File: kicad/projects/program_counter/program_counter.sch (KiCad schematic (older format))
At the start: 47 parts, among them J1 Conn_01x16_Female, J2 Control_signal_backplane, J3 Bus_connection, J4 Aux_connection, J5 LED_CONTROL, J6 TOP_POWER, U1 74HC04, U2 74HC245, U3 74HC161, U4 74HC245, U5 74HC161, U6 74HC245, U7 74HC161, U8 74HC245, U9 74HC161

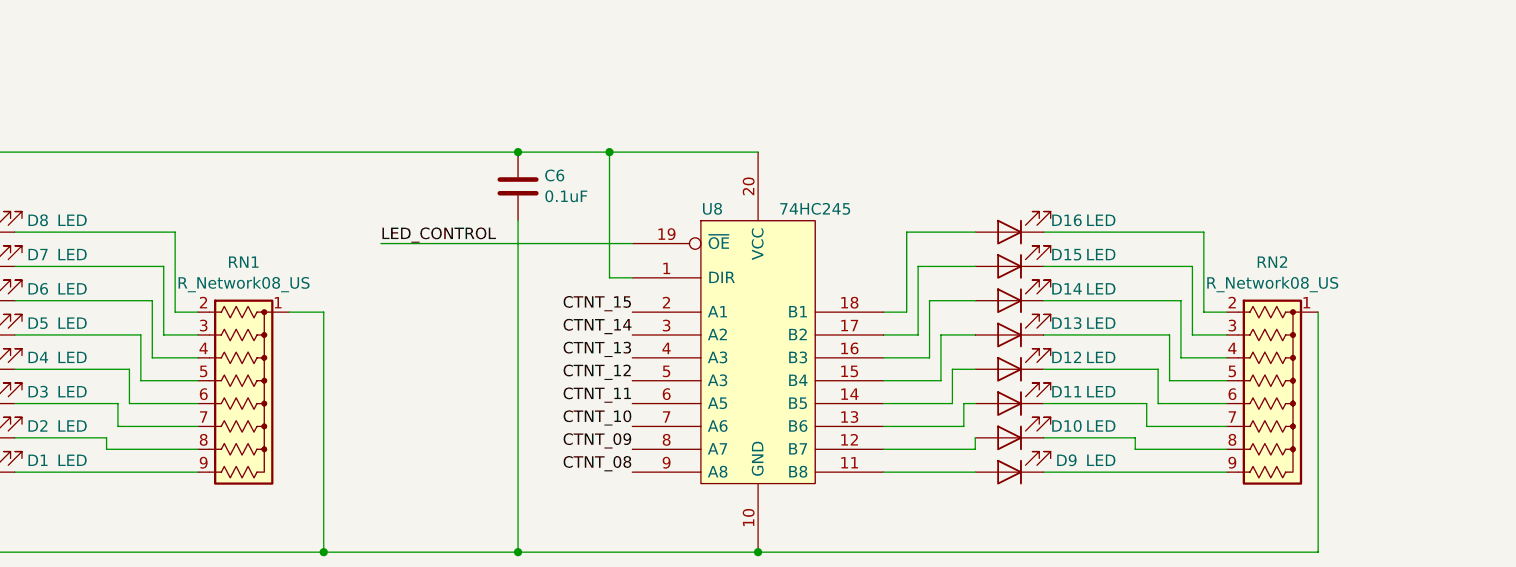
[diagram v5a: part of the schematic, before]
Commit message: Tech checks complete on program counter.
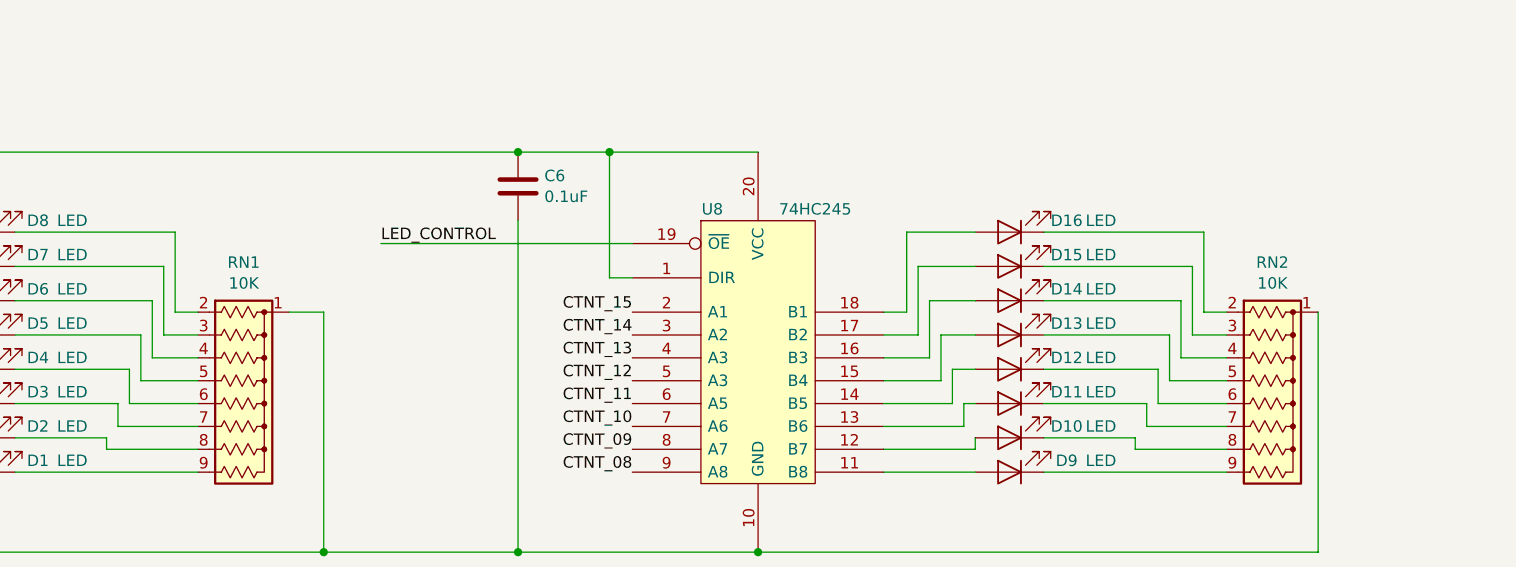
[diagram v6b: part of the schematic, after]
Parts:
- RN1, RN2: value R_Network08_US -> 10K
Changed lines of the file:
@@
 P 9200 9400
 F 0 "RN2" V 8583 9400 50  0000 C CNN
-F 1 "R_Network08_US" V 8674 9400 50  0000 C CNN
+F 1 "10K" V 8674 9400 50  0000 C CNN
 F 2 "Resistor_THT:R_Array_SIP9" V 9675 9400 50  0001 C CNN
 F 3 "http://www.vishay.com/docs/31509/csc.pdf" H 9200 9400 50  0001 C CNN
@@
 P 4700 9400
 F 0 "RN1" V 4083 9400 50  0000 C CNN
-F 1 "R_Network08_US" V 4174 9400 50  0000 C CNN
+F 1 "10K" V 4174 9400 50  0000 C CNN
 F 2 "Resistor_THT:R_Array_SIP9" V 5175 9400 50  0001 C CNN
 F 3 "http://www.vishay.com/docs/31509/csc.pdf" H 4700 9400 50  0001 C CNN

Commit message: Gerbers generated and zipped. Changed ICs to sockets.
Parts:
- U1: footprint Package_DIP:DIP-14_W7.62mm -> Package_DIP:DIP-14_W7.62mm_Socket
- U2, U4, U6, U8: footprint Package_DIP:DIP-20_W7.62mm -> Package_DIP:DIP-20_W7.62mm_Socket
- U3, U5, U7, U9: footprint Package_DIP:DIP-16_W7.62mm -> Package_DIP:DIP-16_W7.62mm_Socket
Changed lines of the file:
@@
 F 0 "U6" H 6450 6700 50  0000 C CNN
 F 1 "74HC245" H 6950 6700 50  0000 C CNN
-F 2 "Package_DIP:DIP-20_W7.62mm" H 6350 6000 50  0001 C CNN
+F 2 "Package_DIP:DIP-20_W7.62mm_Socket" H 6350 6000 50  0001 C CNN
 F 3 "" H 6350 6000 50  0001 C CNN
 	1    6700 6000
@@
 F 0 "U4" H 4400 6700 50  0000 C CNN
 F 1 "74HC245" H 4850 6700 50  0000 C CNN
-F 2 "Package_DIP:DIP-20_W7.62mm" H 4250 6000 50  0001 C CNN
+F 2 "Package_DIP:DIP-20_W7.62mm_Socket" H 4250 6000 50  0001 C CNN
 F 3 "" H 4250 6000 50  0001 C CNN
 	1    4600 6000
@@
 F 0 "U1" H 1400 3417 50  0000 C CNN
 F 1 "74HC04" H 1400 3326 50  0000 C CNN
-F 2 "Package_DIP:DIP-14_W7.62mm" H 1400 3100 50  0001 C CNN
+F 2 "Package_DIP:DIP-14_W7.62mm_Socket" H 1400 3100 50  0001 C CNN
 F 3 "https://assets.nexperia.com/documents/data-sheet/74HC_HCT04.pdf" H 1400 3100 50  0001 C CNN
 	1    1400 3100
@@
 F 0 "U1" H 1400 3967 50  0000 C CNN
 F 1 "74HC04" H 1400 3876 50  0000 C CNN
-F 2 "Package_DIP:DIP-14_W7.62mm" H 1400 3650 50  0001 C CNN
+F 2 "Package_DIP:DIP-14_W7.62mm_Socket" H 1400 3650 50  0001 C CNN
 F 3 "https://assets.nexperia.com/documents/data-sheet/74HC_HCT04.pdf" H 1400 3650 50  0001 C CNN
 	2    1400 3650
@@
 F 0 "U1" H 1750 5267 50  0000 C CNN
 F 1 "74HC04" H 1750 5176 50  0000 C CNN
-F 2 "Package_DIP:DIP-14_W7.62mm" H 1750 4950 50  0001 C CNN
+F 2 "Package_DIP:DIP-14_W7.62mm_Socket" H 1750 4950 50  0001 C CNN
 F 3 "https://assets.nexperia.com/documents/data-sheet/74HC_HCT04.pdf" H 1750 4950 50  0001 C CNN
 	3    1750 4950
@@
 F 0 "U1" H 12500 2167 50  0000 C CNN
 F 1 "74HC04" H 12500 2076 50  0000 C CNN
-F 2 "Package_DIP:DIP-14_W7.62mm" H 12500 1850 50  0001 C CNN
+F 2 "Package_DIP:DIP-14_W7.62mm_Socket" H 12500 1850 50  0001 C CNN
 F 3 "https://assets.nexperia.com/documents/data-sheet/74HC_HCT04.pdf" H 12500 1850 50  0001 C CNN
 	4    12500 1850
@@
 F 0 "U1" H 12500 2717 50  0000 C CNN
 F 1 "74HC04" H 12500 2626 50  0000 C CNN
-F 2 "Package_DIP:DIP-14_W7.62mm" H 12500 2400 50  0001 C CNN
+F 2 "Package_DIP:DIP-14_W7.62mm_Socket" H 12500 2400 50  0001 C CNN
 F 3 "https://assets.nexperia.com/documents/data-sheet/74HC_HCT04.pdf" H 12500 2400 50  0001 C CNN
 	5    12500 2400
@@
 F 0 "U1" H 12500 3267 50  0000 C CNN
 F 1 "74HC04" H 12500 3176 50  0000 C CNN
-F 2 "Package_DIP:DIP-14_W7.62mm" H 12500 2950 50  0001 C CNN
+F 2 "Package_DIP:DIP-14_W7.62mm_Socket" H 12500 2950 50  0001 C CNN
 F 3 "https://assets.nexperia.com/documents/data-sheet/74HC_HCT04.pdf" H 12500 2950 50  0001 C CNN
 	6    12500 2950
@@
 F 0 "U1" H 11730 2496 50  0000 L CNN
 F 1 "74HC04" H 11730 2405 50  0000 L CNN
-F 2 "Package_DIP:DIP-14_W7.62mm" H 11500 2450 50  0001 C CNN
+F 2 "Package_DIP:DIP-14_W7.62mm_Socket" H 11500 2450 50  0001 C CNN
 F 3 "https://assets.nexperia.com/documents/data-sheet/74HC_HCT04.pdf" H 11500 2450 50  0001 C CNN
 	7    11500 2450
@@
 F 0 "U2" H 2250 9950 50  0000 C CNN
 F 1 "74HC245" H 2700 9950 50  0000 C CNN
-F 2 "Package_DIP:DIP-20_W7.62mm" H 2100 9250 50  0001 C CNN
+F 2 "Package_DIP:DIP-20_W7.62mm_Socket" H 2100 9250 50  0001 C CNN
 F 3 "" H 2100 9250 50  0001 C CNN
 	1    2450 9250
@@
 F 0 "U8" H 6750 9950 50  0000 C CNN
 F 1 "74HC245" H 7200 9950 50  0000 C CNN
-F 2 "Package_DIP:DIP-20_W7.62mm" H 6600 9250 50  0001 C CNN
+F 2 "Package_DIP:DIP-20_W7.62mm_Socket" H 6600 9250 50  0001 C CNN
 F 3 "" H 6600 9250 50  0001 C CNN
 	1    6950 9250
@@
 F 0 "U3" H 2950 3100 50  0000 C CNN
 F 1 "74HC161" H 3450 3100 50  0000 C CNN
-F 2 "Package_DIP:DIP-16_W7.62mm" H 3200 2450 50  0001 C CNN
+F 2 "Package_DIP:DIP-16_W7.62mm_Socket" H 3200 2450 50  0001 C CNN
 F 3 "https://www.ti.com/lit/ds/symlink/cd54hc163.pdf" H 3200 2450 50  0001 C CNN
 	1    3200 2450
@@
 F 0 "U5" H 4800 3100 50  0000 C CNN
 F 1 "74HC161" H 5300 3100 50  0000 C CNN
-F 2 "Package_DIP:DIP-16_W7.62mm" H 5050 2450 50  0001 C CNN
+F 2 "Package_DIP:DIP-16_W7.62mm_Socket" H 5050 2450 50  0001 C CNN
 F 3 "https://www.ti.com/lit/ds/symlink/cd54hc163.pdf" H 5050 2450 50  0001 C CNN
 	1    5050 2450
@@
 F 0 "U7" H 6650 3100 50  0000 C CNN
 F 1 "74HC161" H 7150 3100 50  0000 C CNN
-F 2 "Package_DIP:DIP-16_W7.62mm" H 6900 2450 50  0001 C CNN
+F 2 "Package_DIP:DIP-16_W7.62mm_Socket" H 6900 2450 50  0001 C CNN
 F 3 "https://www.ti.com/lit/ds/symlink/cd54hc163.pdf" H 6900 2450 50  0001 C CNN
 	1    6900 2450
@@
 F 0 "U9" H 8500 3100 50  0000 C CNN
 F 1 "74HC161" H 9000 3100 50  0000 C CNN
-F 2 "Package_DIP:DIP-16_W7.62mm" H 8750 2450 50  0001 C CNN
+F 2 "Package_DIP:DIP-16_W7.62mm_Socket" H 8750 2450 50  0001 C CNN
 F 3 "https://www.ti.com/lit/ds/symlink/cd54hc163.pdf" H 8750 2450 50  0001 C CNN
 	1    8750 2450
